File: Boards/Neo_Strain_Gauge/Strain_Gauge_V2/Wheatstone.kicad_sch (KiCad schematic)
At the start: 6 parts, among them J1 Screw_Terminal_01x03

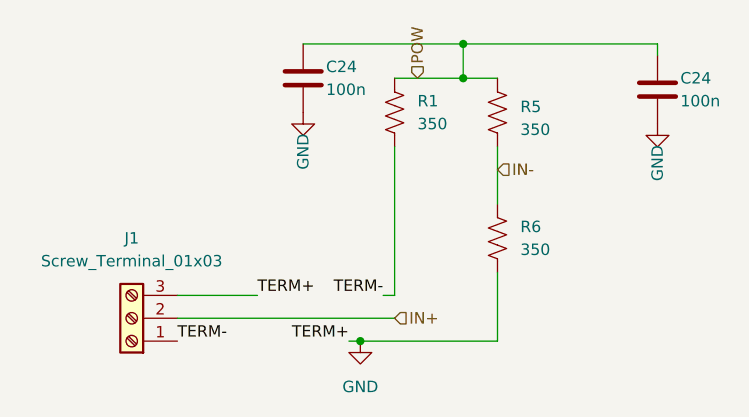
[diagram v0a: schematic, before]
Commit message: Updated strain gauge V2 to have a button
I need to update the button to be closer to ones we already have however.
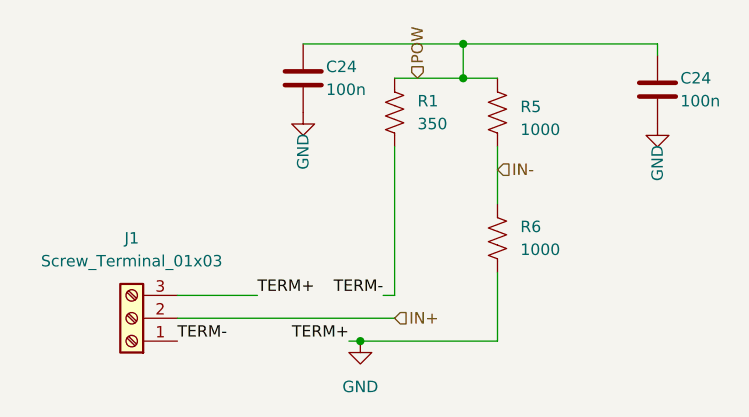
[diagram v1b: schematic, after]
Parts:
- R5, R6: value 350 -> 1000; Purchase Link https://www.digikey.com/en/products/detail/vishay-dale-thin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 -> https://www.digikey.com/en/products/detail/koa-speer-electr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
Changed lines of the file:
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@@
       (effects (font (size 1.27 1.27)) (justify left))
     )
-    (property "Value" "350" (at 102.87 69.8499 0)
+    (property "Value" "1000" (at 102.87 69.8499 0)
       (effects (font (size 1.27 1.27)) (justify left))
     )
@@
       (effects (font (size 1.27 1.27)) hide)
     )
-    (property "Purchase Link" "https://www.digikey.com/en/products/detail/vishay-dale-thin-film/D55342E07B350ART5/3197959" (at 100.33 68.58 0)
+    (property "Purchase Link" "https://www.digikey.com/en/products/detail/koa-speer-electronics-inc/RN73R2BTTD1001B25/10038824" (at 100.33 68.58 0)
       (effects (font (size 1.27 1.27)) hide)
     )
@@
       (effects (font (size 1.27 1.27)) (justify left))
     )
-    (property "Value" "350" (at 102.87 56.515 0)
+    (property "Value" "1000" (at 102.87 56.515 0)
       (effects (font (size 1.27 1.27)) (justify left))
     )
@@
       (effects (font (size 1.27 1.27)) hide)
     )
-    (property "Purchase Link" "https://www.digikey.com/en/products/detail/vishay-dale-thin-film/D55342E07B350ART5/3197959" (at 100.33 54.61 0)
-      (effects (font (size 1.27 1.27)) hide)
-    )
+    (property "Purchase Link" "https://www.digikey.com/en/products/detail/koa-speer-electronics-inc/RN73R2BTTD1001B25/10038824" (at 100.33 54.61 0)
+      (effects (font (size 1.27 1.27)) hide)
+    )
